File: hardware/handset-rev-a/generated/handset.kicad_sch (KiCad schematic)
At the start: 0 parts

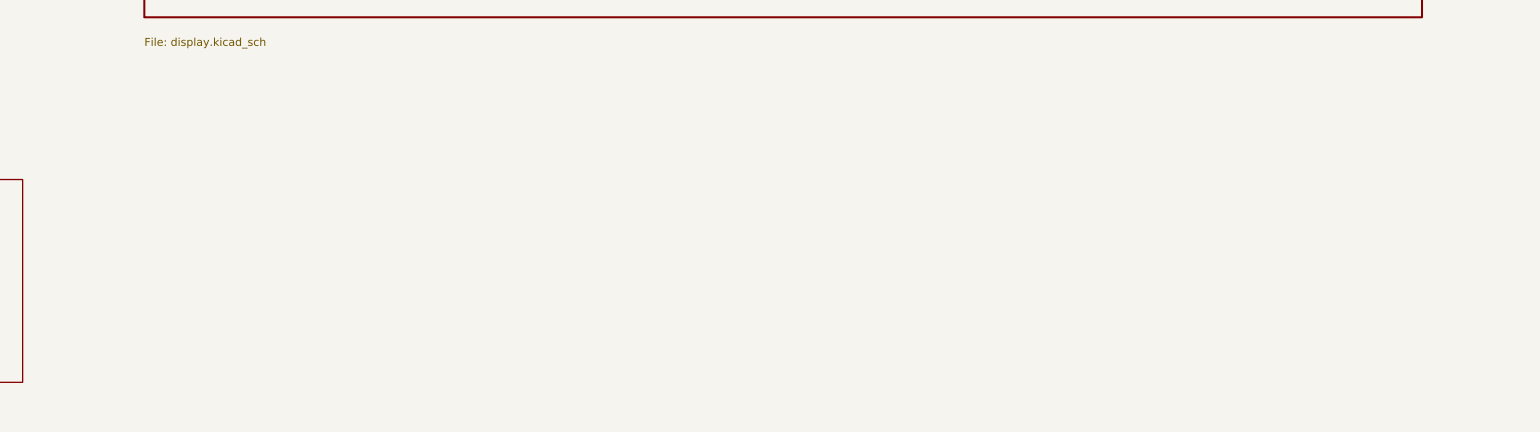
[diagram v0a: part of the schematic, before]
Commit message: feat: add expansion power and signal control
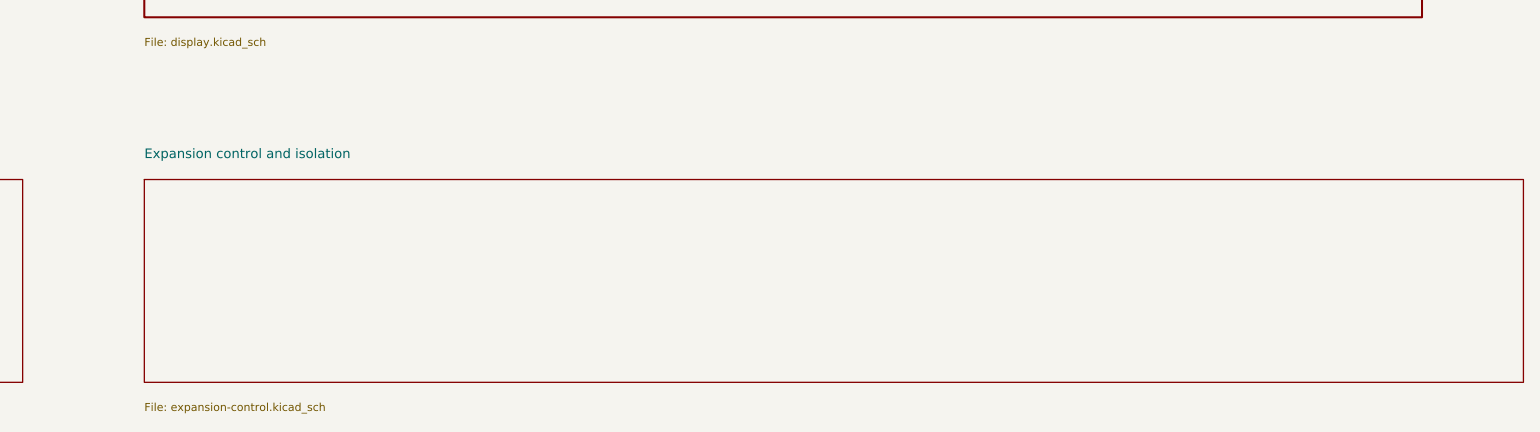
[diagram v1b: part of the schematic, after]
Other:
- added sheet Expansion control and isolation (expansion-control.kicad_sch)
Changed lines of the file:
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@@
       (project "handset"
         (path "/4170cf98-dd26-5fa4-8ee5-b0af1f1df8d5"
-          (page "24"))))))
+          (page "24")))))
+  (sheet
+    (at 401.32 365.76)
+    (size 172.72 25.4)
+    (stroke
+      (width 0.1524)
+      (type solid))
+    (fill
+      (color 0 0 0 0))
+    (property "Sheetname" "Expansion control and isolation"
+      (at 401.32 363.22 0)
+      (effects
+        (font
+          (size 1.2 1.2))
+        (justify left bottom)))
+    (property "Sheetfile" "expansion-control.kicad_sch"
+      (at 401.32 393.7 0)
+      (effects
+        (font
+          (size 1 1))
+        (justify left top)))
+    (instances
+      (project "handset"
+        (path "/4170cf98-dd26-5fa4-8ee5-b0af1f1df8d5"
+          (page "25"))))))
